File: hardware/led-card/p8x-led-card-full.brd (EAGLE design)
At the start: 160 x 100 mm, 19 parts, among them J1 FABC96R, U1 74HCT30, U2 74HCT138, U3 74HCT138, U4 74HCT32, U5 74HCT14, U6 74HCT374

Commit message: feat(hardware): use con-vg DIN 41612 footprints (MABC96R card / FABC96S backplane)
Replace the hand-rolled DIN96/DIN96C connector packages with the real Eagle
con-vg DIN 41612 footprints (geometry baked into the generator so it stays
self-contained): card edge = MABC96R (male right-angle), backplane = FABC96S
(female vertical) — both A/B/C @ 2.54mm, drill 0.9144, two M2.5 mounting holes
at y=+/-45. Card value -> MABC96R; pin->pad names unchanged (A1..C32) so the
netlist is intact.

con-vg centres the pad field on the element origin, so the backplane (hand-
placed/routed) was re-derived: slots dropped to y=54.6 to centre the pin field
on the 109mm board (pads now on-board), bus traces re-routed to the new A/B/C
columns (element at sx(i)-2.54). Cards auto-adapt via fp_box. All 8 boards
validate (0 errors).

Known: 3 placement-overlap WARNINGS on the backplane (power-LED resistor; CT2/RT1
clock terminators, both DNP) where the taller connector crowds the top/bottom
strips — to clear during the Fusion placement pass.

Co-Authored-By: Claude Opus 4.8 <noreply@anthropic.com>
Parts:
- J1: value FABC96R -> MABC96R; device p8x:DIN96C -> p8x:MABC96R
- moved J1 37.5 mm to (7.94, 49.6)

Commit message: feat(hardware): 100nF bypass caps to 0.1" lead pitch on all boards
The 100nF ceramic-disc decoupling/bypass caps used the shared C_DISC footprint
at 0.2" (5.08mm) lead spacing. The parts being sourced are 0.1" (2.54mm) pitch,
so retarget just those caps:

- Add a C_DISC1 footprint (pad 2 at y=-2.54) and a CAP1 device that reuses the
  CAP schematic symbol art but points at C_DISC1.
- Route the 100nF parts to CAP1: per-IC decoupling (CDn), the placement-flow
  copies, and the backplane per-slot caps C1-C10.
- Leave C_DISC (0.2") for the parts that still use it: the 1uF caps, the 150pF
  clock terminators (CT1/CT2), and the XTAL32 placeholder.

Regenerated all 8 boards (.sch/.brd/-full.brd) and the schematic PDFs; the
narrower pad field also relieves the backplane connector clearance. Validation:
0 errors on all boards.

Co-Authored-By: Claude Opus 4.8 <noreply@anthropic.com>
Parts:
- CD1, CD2, CD3, CD4, CD5, CD6: device p8x:C_DISC -> p8x:C_DISC1
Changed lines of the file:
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@@
 <attribute name="VALUE" x="17.87" y="92.66" size="1.778" layer="27" ratio="10"/>
 </element>
-<element name="CD1" library="p8x" package="C_DISC" value="100N" x="29.79" y="95.10" smashed="yes">
+<element name="CD1" library="p8x" package="C_DISC1" value="100N" x="29.79" y="95.10" smashed="yes">
 <attribute name="NAME" x="29.79" y="97.64" size="1.778" layer="25" ratio="10"/>
 <attribute name="VALUE" x="29.79" y="92.56" size="1.778" layer="27" ratio="10"/>
@@
 <attribute name="VALUE" x="34.09" y="92.66" size="1.778" layer="27" ratio="10"/>
 </element>
-<element name="CD2" library="p8x" package="C_DISC" value="100N" x="46.01" y="95.10" smashed="yes">
+<element name="CD2" library="p8x" package="C_DISC1" value="100N" x="46.01" y="95.10" smashed="yes">
 <attribute name="NAME" x="46.01" y="97.64" size="1.778" layer="25" ratio="10"/>
 <attribute name="VALUE" x="46.01" y="92.56" size="1.778" layer="27" ratio="10"/>
@@
 <attribute name="VALUE" x="50.31" y="92.66" size="1.778" layer="27" ratio="10"/>
 </element>
-<element name="CD3" library="p8x" package="C_DISC" value="100N" x="62.23" y="95.10" smashed="yes">
+<element name="CD3" library="p8x" package="C_DISC1" value="100N" x="62.23" y="95.10" smashed="yes">
 <attribute name="NAME" x="62.23" y="97.64" size="1.778" layer="25" ratio="10"/>
 <attribute name="VALUE" x="62.23" y="92.56" size="1.778" layer="27" ratio="10"/>
@@
 <attribute name="VALUE" x="66.53" y="92.66" size="1.778" layer="27" ratio="10"/>
 </element>
-<element name="CD4" library="p8x" package="C_DISC" value="100N" x="78.45" y="95.10" smashed="yes">
+<element name="CD4" library="p8x" package="C_DISC1" value="100N" x="78.45" y="95.10" smashed="yes">
 <attribute name="NAME" x="78.45" y="97.64" size="1.778" layer="25" ratio="10"/>
 <attribute name="VALUE" x="78.45" y="92.56" size="1.778" layer="27" ratio="10"/>
@@
 <attribute name="VALUE" x="82.75" y="92.66" size="1.778" layer="27" ratio="10"/>
 </element>
-<element name="CD5" library="p8x" package="C_DISC" value="100N" x="94.67" y="95.10" smashed="yes">
+<element name="CD5" library="p8x" package="C_DISC1" value="100N" x="94.67" y="95.10" smashed="yes">
 <attribute name="NAME" x="94.67" y="97.64" size="1.778" layer="25" ratio="10"/>
 <attribute name="VALUE" x="94.67" y="92.56" size="1.778" layer="27" ratio="10"/>
@@
 <attribute name="VALUE" x="98.97" y="92.66" size="1.778" layer="27" ratio="10"/>
 </element>
-<element name="CD6" library="p8x" package="C_DISC" value="100N" x="110.89" y="95.10" smashed="yes">
+<element name="CD6" library="p8x" package="C_DISC1" value="100N" x="110.89" y="95.10" smashed="yes">
 <attribute name="NAME" x="110.89" y="97.64" size="1.778" layer="25" ratio="10"/>
 <attribute name="VALUE" x="110.89" y="92.56" size="1.778" layer="27" ratio="10"/>

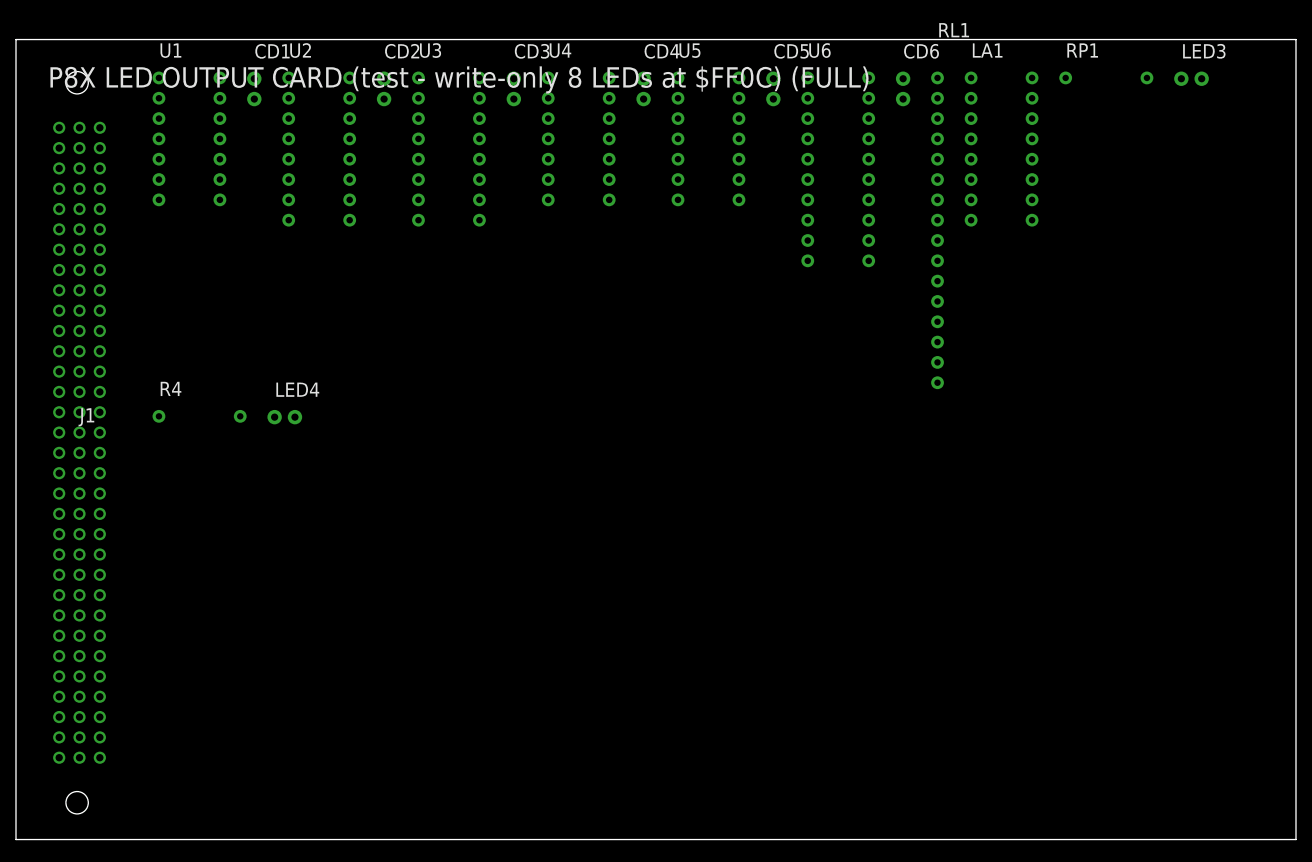
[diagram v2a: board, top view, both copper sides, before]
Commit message: hardware: silkscreen off footprints, standard cap value format, backplane RL1->R1
Pre-Fusion cleanup so there is less to fix by hand once placing/routing.

1. SILKSCREEN NO LONGER OVERLAYS FOOTPRINTS (all boards). NAME/VALUE were emitted
   at the element origin +/-2.54 regardless of part size, so on anything bigger
   than a 2-pin part the text landed ON the pads -- the 96-pin DIN connector had
   J1/SLOT1 across its pad field, and caps had their values on top of them. Now
   placed against the real footprint bbox (fp_box): NAME 0.7mm above the top edge,
   VALUE 0.7mm below the bottom, left-aligned to the box. Verified: 1642
   silkscreen labels across all 9 boards, 0 sitting on a footprint (was many).
   Not rotation-aware, which is fine -- no board rotates a part today.

2. CAPACITOR VALUES use standard unit suffixes: 100N->100nF, 470U->470uF,
   150P->150pF, 1U->1uF (and the DNP/x10 variants). Applied everywhere, so the
   per-IC decoupling caps on every card change too. No doc quoted the raw value
   strings, so no doc churn.

3. BACKPLANE RL1 -> R1 (standard R designator). Scoped to the backplane section
   only -- the io-card and led-card have their own unrelated RL1 (8x330R networks)
   which are untouched. Backplane theory/design docs updated to match.

Part refs/values are decided in gen_eagle.py: the backplane `small=[...]` list and
each cards `ic`/`sm` dicts.

Co-Authored-By: Claude Opus 4.8 <noreply@anthropic.com>
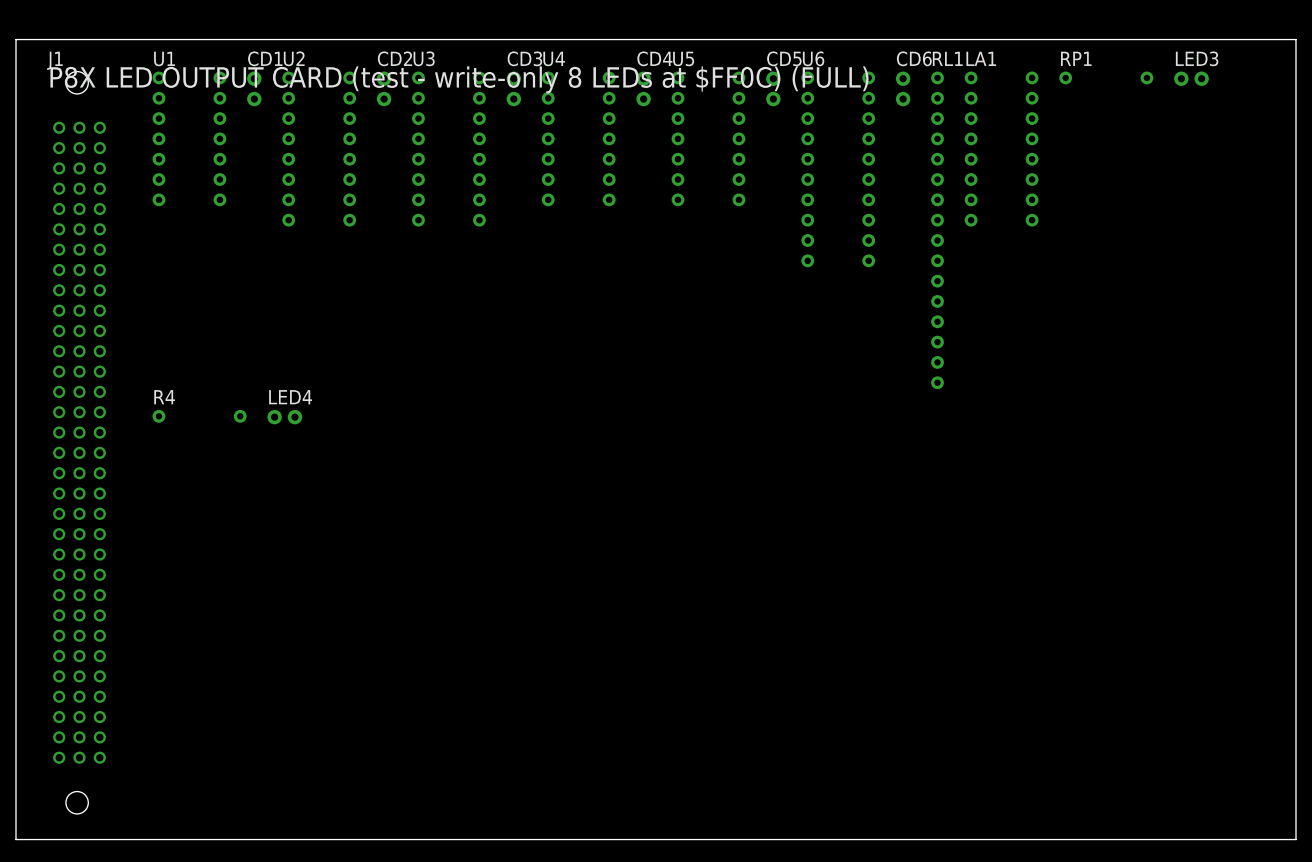
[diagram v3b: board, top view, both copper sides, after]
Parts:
- CD1, CD2, CD3, CD4, CD5, CD6: value 100N -> 100nF
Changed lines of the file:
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@@
 <elements>
 <element name="J1" library="p8x" package="MABC96R" value="MABC96R" x="7.94" y="49.60" smashed="yes">
-<attribute name="NAME" x="7.94" y="52.14" size="1.778" layer="25" ratio="10"/>
-<attribute name="VALUE" x="7.94" y="47.06" size="1.778" layer="27" ratio="10"/>
+<attribute name="NAME" x="4.00" y="96.70" size="1.778" layer="25" ratio="10"/>
+<attribute name="VALUE" x="4.00" y="0.73" size="1.778" layer="27" ratio="10"/>
 </element>
 <element name="U1" library="p8x" package="DIP14" value="74HCT30" x="17.87" y="95.20" smashed="yes">
-<attribute name="NAME" x="17.87" y="97.74" size="1.778" layer="25" ratio="10"/>
-<attribute name="VALUE" x="17.87" y="92.66" size="1.778" layer="27" ratio="10"/>
+<attribute name="NAME" x="17.07" y="96.70" size="1.778" layer="25" ratio="10"/>
+<attribute name="VALUE" x="17.07" y="76.68" size="1.778" layer="27" ratio="10"/>
 </element>
-<element name="CD1" library="p8x" package="C_DISC1" value="100N" x="29.79" y="95.10" smashed="yes">
-<attribute name="NAME" x="29.79" y="97.64" size="1.778" layer="25" ratio="10"/>
-<attribute name="VALUE" x="29.79" y="92.56" size="1.778" layer="27" ratio="10"/>
+<element name="CD1" library="p8x" package="C_DISC1" value="100nF" x="29.79" y="95.10" smashed="yes">
+<attribute name="NAME" x="28.89" y="96.70" size="1.778" layer="25" ratio="10"/>
+<attribute name="VALUE" x="28.89" y="89.18" size="1.778" layer="27" ratio="10"/>
 </element>
 <element name="U2" library="p8x" package="DIP16" value="74HCT138" x="34.09" y="95.20" smashed="yes">
-<attribute name="NAME" x="34.09" y="97.74" size="1.778" layer="25" ratio="10"/>
-<attribute name="VALUE" x="34.09" y="92.66" size="1.778" layer="27" ratio="10"/>
+<attribute name="NAME" x="33.29" y="96.70" size="1.778" layer="25" ratio="10"/>
+<attribute name="VALUE" x="33.29" y="74.14" size="1.778" layer="27" ratio="10"/>
 </element>
-<element name="CD2" library="p8x" package="C_DISC1" value="100N" x="46.01" y="95.10" smashed="yes">
-<attribute name="NAME" x="46.01" y="97.64" size="1.778" layer="25" ratio="10"/>
-<attribute name="VALUE" x="46.01" y="92.56" size="1.778" layer="27" ratio="10"/>
+<element name="CD2" library="p8x" package="C_DISC1" value="100nF" x="46.01" y="95.10" smashed="yes">
+<attribute name="NAME" x="45.11" y="96.70" size="1.778" layer="25" ratio="10"/>
+<attribute name="VALUE" x="45.11" y="89.18" size="1.778" layer="27" ratio="10"/>
 </element>
 <element name="U3" library="p8x" package="DIP16" value="74HCT138" x="50.31" y="95.20" smashed="yes">
-<attribute name="NAME" x="50.31" y="97.74" size="1.778" layer="25" ratio="10"/>
-<attribute name="VALUE" x="50.31" y="92.66" size="1.778" layer="27" ratio="10"/>
+<attribute name="NAME" x="49.51" y="96.70" size="1.778" layer="25" ratio="10"/>
+<attribute name="VALUE" x="49.51" y="74.14" size="1.778" layer="27" ratio="10"/>
 </element>
-<element name="CD3" library="p8x" package="C_DISC1" value="100N" x="62.23" y="95.10" smashed="yes">
-<attribute name="NAME" x="62.23" y="97.64" size="1.778" layer="25" ratio="10"/>
-<attribute name="VALUE" x="62.23" y="92.56" size="1.778" layer="27" ratio="10"/>
+<element name="CD3" library="p8x" package="C_DISC1" value="100nF" x="62.23" y="95.10" smashed="yes">
+<attribute name="NAME" x="61.33" y="96.70" size="1.778" layer="25" ratio="10"/>
+<attribute name="VALUE" x="61.33" y="89.18" size="1.778" layer="27" ratio="10"/>
 </element>
 <element name="U4" library="p8x" package="DIP14" value="74HCT32" x="66.53" y="95.20" smashed="yes">
-<attribute name="NAME" x="66.53" y="97.74" size="1.778" layer="25" ratio="10"/>
-<attribute name="VALUE" x="66.53" y="92.66" size="1.778" layer="27" ratio="10"/>
+<attribute name="NAME" x="65.73" y="96.70" size="1.778" layer="25" ratio="10"/>
+<attribute name="VALUE" x="65.73" y="76.68" size="1.778" layer="27" ratio="10"/>
 </element>
-<element name="CD4" library="p8x" package="C_DISC1" value="100N" x="78.45" y="95.10" smashed="yes">
-<attribute name="NAME" x="78.45" y="97.64" size="1.778" layer="25" ratio="10"/>
-<attribute name="VALUE" x="78.45" y="92.56" size="1.778" layer="27" ratio="10"/>
+<element name="CD4" library="p8x" package="C_DISC1" value="100nF" x="78.45" y="95.10" smashed="yes">
+<attribute name="NAME" x="77.55" y="96.70" size="1.778" layer="25" ratio="10"/>
+<attribute name="VALUE" x="77.55" y="89.18" size="1.778" layer="27" ratio="10"/>
 </element>
 <element name="U5" library="p8x" package="DIP14" value="74HCT14" x="82.75" y="95.20" smashed="yes">
-<attribute name="NAME" x="82.75" y="97.74" size="1.778" layer="25" ratio="10"/>
-<attribute name="VALUE" x="82.75" y="92.66" size="1.778" layer="27" ratio="10"/>
+<attribute name="NAME" x="81.95" y="96.70" size="1.778" layer="25" ratio="10"/>
+<attribute name="VALUE" x="81.95" y="76.68" size="1.778" layer="27" ratio="10"/>
 </element>
-<element name="CD5" library="p8x" package="C_DISC1" value="100N" x="94.67" y="95.10" smashed="yes">
-<attribute name="NAME" x="94.67" y="97.64" size="1.778" layer="25" ratio="10"/>
-<attribute name="VALUE" x="94.67" y="92.56" size="1.778" layer="27" ratio="10"/>
+<element name="CD5" library="p8x" package="C_DISC1" value="100nF" x="94.67" y="95.10" smashed="yes">
+<attribute name="NAME" x="93.77" y="96.70" size="1.778" layer="25" ratio="10"/>
+<attribute name="VALUE" x="93.77" y="89.18" size="1.778" layer="27" ratio="10"/>
 </element>
 <element name="U6" library="p8x" package="DIP20" value="74HCT374" x="98.97" y="95.20" smashed="yes">
-<attribute name="NAME" x="98.97" y="97.74" size="1.778" layer="25" ratio="10"/>
-<attribute name="VALUE" x="98.97" y="92.66" size="1.778" layer="27" ratio="10"/>
+<attribute name="NAME" x="98.17" y="96.70" size="1.778" layer="25" ratio="10"/>
+<attribute name="VALUE" x="98.17" y="69.06" size="1.778" layer="27" ratio="10"/>
 </element>
-<element name="CD6" library="p8x" package="C_DISC1" value="100N" x="110.89" y="95.10" smashed="yes">
-<attribute name="NAME" x="110.89" y="97.64" size="1.778" layer="25" ratio="10"/>
-<attribute name="VALUE" x="110.89" y="92.56" size="1.778" layer="27" ratio="10"/>
+<element name="CD6" library="p8x" package="C_DISC1" value="100nF" x="110.89" y="95.10" smashed="yes">
+<attribute name="NAME" x="109.99" y="96.70" size="1.778" layer="25" ratio="10"/>
+<attribute name="VALUE" x="109.99" y="89.18" size="1.778" layer="27" ratio="10"/>
 </element>
 <element name="RL1" library="p8x" package="SIP16" value="8x330R" x="115.19" y="97.74" smashed="yes">
-<attribute name="NAME" x="115.19" y="100.28" size="1.778" layer="25" ratio="10"/>
-<attribute name="VALUE" x="115.19" y="95.20" size="1.778" layer="27" ratio="10"/>
+<attribute name="NAME" x="114.39" y="96.70" size="1.778" layer="25" ratio="10"/>
+<attribute name="VALUE" x="114.39" y="53.82" size="1.778" layer="27" ratio="10"/>
 </element>
 <element name="LA1" library="p8x" package="DIP16" value="8-LED BAR" x="119.39" y="95.20" smashed="yes">
-<attribute name="NAME" x="119.39" y="97.74" size="1.778" layer="25" ratio="10"/>
-<attribute name="VALUE" x="119.39" y="92.66" size="1.778" layer="27" ratio="10"/>
+<attribute name="NAME" x="118.59" y="96.70" size="1.778" layer="25" ratio="10"/>
+<attribute name="VALUE" x="118.59" y="74.14" size="1.778" layer="27" ratio="10"/>
 </element>
 <element name="RP1" library="p8x" package="R_AXIAL" value="1K" x="131.21" y="95.20" smashed="yes">
-<attribute name="NAME" x="131.21" y="97.74" size="1.778" layer="25" ratio="10"/>
-<attribute name="VALUE" x="131.21" y="92.66" size="1.778" layer="27" ratio="10"/>
+<attribute name="NAME" x="130.41" y="96.70" size="1.778" layer="25" ratio="10"/>
+<attribute name="VALUE" x="130.41" y="91.92" size="1.778" layer="27" ratio="10"/>
 </element>
 <element name="LED3" library="p8x" package="LED5" value="GRN" x="145.67" y="95.10" smashed="yes">
-<attribute name="NAME" x="145.67" y="97.64" size="1.778" layer="25" ratio="10"/>
-<attribute name="VALUE" x="145.67" y="92.56" size="1.778" layer="27" ratio="10"/>
+<attribute name="NAME" x="144.77" y="96.70" size="1.778" layer="25" ratio="10"/>
+<attribute name="VALUE" x="144.77" y="91.72" size="1.778" layer="27" ratio="10"/>
 </element>
 <element name="R4" library="p8x" package="R_AXIAL" value="1K" x="17.87" y="52.90" smashed="yes">
-<attribute name="NAME" x="17.87" y="55.44" size="1.778" layer="25" ratio="10"/>
-<attribute name="VALUE" x="17.87" y="50.36" size="1.778" layer="27" ratio="10"/>
+<attribute name="NAME" x="17.07" y="54.40" size="1.778" layer="25" ratio="10"/>
+<attribute name="VALUE" x="17.07" y="49.62" size="1.778" layer="27" ratio="10"/>
 </element>
 <element name="LED4" library="p8x" package="LED5" value="YEL" x="32.33" y="52.80" smashed="yes">
-<attribute name="NAME" x="32.33" y="55.34" size="1.778" layer="25" ratio="10"/>
-<attribute name="VALUE" x="32.33" y="50.26" size="1.778" layer="27" ratio="10"/>
+<attribute name="NAME" x="31.43" y="54.40" size="1.778" layer="25" ratio="10"/>
+<attribute name="VALUE" x="31.43" y="49.42" size="1.778" layer="27" ratio="10"/>
 </element>
 </elements><signals>
